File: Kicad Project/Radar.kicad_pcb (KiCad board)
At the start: 2 copper layers, 104.1 x 101.6 mm, 46 parts, among them U1 GALI-1+, U10 GALI-2+, U2 MCA1-85L+, U4 LMV751, U5 LMV751, U6 GALI-2+, U7 RMK-3-93+, U8 GALI-2+, U9 LEE-39+

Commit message: asdf
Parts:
- moved R19 53.5 mm to (163.8, 143.5)
- moved R18 53.1 mm to (181.6, 143.5)
- moved C12 41.8 mm to (134.6, 154.9)
- moved R15 37.8 mm to (147.3, 166.4)
- moved U10 23.8 mm to (185.4, 133.3), turned to 270 degrees
- moved C14 21.6 mm to (188.0, 151.1), turned to 90 degrees
- moved C13 6.62 mm to (174.0, 135.9), turned to 90 degrees
- moved C11 6.00 mm to (188.0, 125.7)
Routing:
- net Net-(C11-Pad1): track 1.23 -> 0.00 mm
- net (no net): track 0.00 -> 1.23 mm
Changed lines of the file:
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@@
     (links 136)
     (no_connects 52)
-    (area 93.904999 76.124999 198.195001 177.875001)
+    (area 93.904999 64.6811 228.422201 177.875001)
     (thickness 1.6)
     (drawings 48)
@@
   )
   (setup
-    (last_trace_width 2.54)
+    (last_trace_width 0.25)
     (user_trace_width 0.254)
     (user_trace_width 0.508)
@@
   )
   (module RadarComponents:Amplifier (layer F.Cu)
-    (at 163.17799 141.9332)
-    (fp_text reference U10 (at -5.9436 -5.9182) (layer F.SilkS)
-      (effects (font (size 1 1) (thickness 0.15)))
-    )
-    (fp_text value GALI-2+ (at 4.1656 -6.1468) (layer F.Fab)
-      (effects (font (size 1 1) (thickness 0.15)))
-    )
-    (pad 2 thru_hole rect (at 0.7874 2.413) (size 1.27 1.27) (drill 0.381) (layers *.Cu *.Mask)
-      (net 9 GND))
-    (pad 2 thru_hole rect (at 2.0574 2.413) (size 1.27 1.27) (drill 0.381) (layers *.Cu *.Mask)
-      (net 9 GND))
-    (pad 2 thru_hole rect (at -0.4826 2.413) (size 1.27 1.27) (drill 0.381) (layers *.Cu *.Mask)
-      (net 9 GND))
-    (pad 2 thru_hole rect (at -0.4826 1.143) (size 1.27 1.27) (drill 0.381) (layers *.Cu *.Mask)
-      (net 9 GND))
-    (pad 2 thru_hole rect (at 0.7874 1.143) (size 1.27 1.27) (drill 0.381) (layers *.Cu *.Mask)
-      (net 9 GND))
-    (pad 2 thru_hole rect (at 2.0574 1.143) (size 1.27 1.27) (drill 0.381) (layers *.Cu *.Mask)
-      (net 9 GND))
-    (pad 2 thru_hole rect (at 2.0828 -4.953) (size 1.27 1.27) (drill 0.381) (layers *.Cu *.Mask)
-      (net 9 GND))
-    (pad 2 thru_hole rect (at 0.8128 -4.953) (size 1.27 1.27) (drill 0.381) (layers *.Cu *.Mask)
-      (net 9 GND))
-    (pad 2 thru_hole rect (at -0.4572 -4.953) (size 1.27 1.27) (drill 0.381) (layers *.Cu *.Mask)
-      (net 9 GND))
-    (pad 2 thru_hole rect (at -0.4572 -3.683) (size 1.27 1.27) (drill 0.381) (layers *.Cu *.Mask)
-      (net 9 GND))
-    (pad 2 thru_hole rect (at 2.0828 -3.683) (size 1.27 1.27) (drill 0.381) (layers *.Cu *.Mask)
-      (net 9 GND))
-    (pad 3 smd rect (at 2.8956 -1.27) (size 2.54 2.54) (layers F.Cu F.Paste F.Mask)
+    (at 185.42 133.35 270)
+    (fp_text reference U10 (at -5.9436 -5.9182 270) (layer F.SilkS)
+      (effects (font (size 1 1) (thickness 0.15)))
+    )
+    (fp_text value GALI-2+ (at 4.1656 -6.1468 270) (layer F.Fab)
+      (effects (font (size 1 1) (thickness 0.15)))
+    )
+    (pad 2 thru_hole rect (at 0.7874 2.413 270) (size 1.27 1.27) (drill 0.381) (layers *.Cu *.Mask)
+      (net 9 GND))
+    (pad 2 thru_hole rect (at 2.0574 2.413 270) (size 1.27 1.27) (drill 0.381) (layers *.Cu *.Mask)
+      (net 9 GND))
+    (pad 2 thru_hole rect (at -0.4826 2.413 270) (size 1.27 1.27) (drill 0.381) (layers *.Cu *.Mask)
+      (net 9 GND))
+    (pad 2 thru_hole rect (at -0.4826 1.143 270) (size 1.27 1.27) (drill 0.381) (layers *.Cu *.Mask)
+      (net 9 GND))
+    (pad 2 thru_hole rect (at 0.7874 1.143 270) (size 1.27 1.27) (drill 0.381) (layers *.Cu *.Mask)
+      (net 9 GND))
+    (pad 2 thru_hole rect (at 2.0574 1.143 270) (size 1.27 1.27) (drill 0.381) (layers *.Cu *.Mask)
+      (net 9 GND))
+    (pad 2 thru_hole rect (at 2.0828 -4.953 270) (size 1.27 1.27) (drill 0.381) (layers *.Cu *.Mask)
+      (net 9 GND))
+    (pad 2 thru_hole rect (at 0.8128 -4.953 270) (size 1.27 1.27) (drill 0.381) (layers *.Cu *.Mask)
+      (net 9 GND))
+    (pad 2 thru_hole rect (at -0.4572 -4.953 270) (size 1.27 1.27) (drill 0.381) (layers *.Cu *.Mask)
+      (net 9 GND))
+    (pad 2 thru_hole rect (at -0.4572 -3.683 270) (size 1.27 1.27) (drill 0.381) (layers *.Cu *.Mask)
+      (net 9 GND))
+    (pad 2 thru_hole rect (at 2.0828 -3.683 270) (size 1.27 1.27) (drill 0.381) (layers *.Cu *.Mask)
+      (net 9 GND))
+    (pad 3 smd rect (at 2.8956 -1.27 270) (size 2.54 2.54) (layers F.Cu F.Paste F.Mask)
       (net 28 "Net-(C14-Pad2)"))
-    (pad 1 smd rect (at -1.27 -1.27) (size 2.54 2.54) (layers F.Cu F.Paste F.Mask)
+    (pad 1 smd rect (at -1.27 -1.27 270) (size 2.54 2.54) (layers F.Cu F.Paste F.Mask)
       (net 17 "Net-(C11-Pad1)"))
-    (pad 2 smd rect (at 0.8128 -1.27) (size 0.635 3.556) (layers F.Cu F.Paste F.Mask)
-      (net 9 GND))
-    (pad 2 thru_hole rect (at 0.8128 -3.683) (size 1.27 1.27) (drill 0.381) (layers *.Cu *.Mask)
+    (pad 2 smd rect (at 0.8128 -1.27 270) (size 0.635 3.556) (layers F.Cu F.Paste F.Mask)
+      (net 9 GND))
+    (pad 2 thru_hole rect (at 0.8128 -3.683 270) (size 1.27 1.27) (drill 0.381) (layers *.Cu *.Mask)
       (net 9 GND))
   )
@@
   )
   (module RadarComponents:100PAD (layer F.Cu)
-    (at 188.5315 131.699 90)
+    (at 187.96 125.73 90)
     (fp_text reference C11 (at -2.9972 -3.683 90) (layer F.SilkS)
       (effects (font (size 1 1) (thickness 0.15)))
@@
   )
   (module RadarComponents:100PAD (layer F.Cu)
-    (at 172.480581 137.2864)
+    (at 134.62 154.94)
     (fp_text reference C12 (at -2.9972 -3.683) (layer F.SilkS)
       (effects (font (size 1 1) (thickness 0.15)))
@@
   )
   (module RadarComponents:100PAD (layer F.Cu)
-    (at 172.480581 142.3364)
-    (fp_text reference C13 (at -2.9972 -3.683) (layer F.SilkS)
-      (effects (font (size 1 1) (thickness 0.15)))
-    )
-    (fp_text value 150p (at 5.842 -3.683) (layer F.Fab)
-      (effects (font (size 1 1) (thickness 0.15)))
-    )
-    (pad 2 smd rect (at 1.9304 -1.27) (size 2.54 2.54) (layers F.Cu F.Paste F.Mask)
-      (net 9 GND))
-    (pad 1 smd rect (at -1.27 -1.27) (size 2.54 2.54) (layers F.Cu F.Paste F.Mask)
+    (at 173.99 135.89 90)
+    (fp_text reference C13 (at -2.9972 -3.683 90) (layer F.SilkS)
+      (effects (font (size 1 1) (thickness 0.15)))
+    )
+    (fp_text value 150p (at 5.842 -3.683 90) (layer F.Fab)
+      (effects (font (size 1 1) (thickness 0.15)))
+    )
+    (pad 2 smd rect (at 1.9304 -1.27 90) (size 2.54 2.54) (layers F.Cu F.Paste F.Mask)
+      (net 9 GND))
+    (pad 1 smd rect (at -1.27 -1.27 90) (size 2.54 2.54) (layers F.Cu F.Paste F.Mask)
       (net 27 "Net-(C13-Pad1)"))
   )
   (module RadarComponents:100PAD (layer F.Cu)
-    (at 175.9712 133.1468)
-    (fp_text reference C14 (at -2.9972 -3.683) (layer F.SilkS)
-      (effects (font (size 1 1) (thickness 0.15)))
-    )
-    (fp_text value 150p (at 5.842 -3.683) (layer F.Fab)
-      (effects (font (size 1 1) (thickness 0.15)))
-    )
-    (pad 2 smd rect (at 1.9304 -1.27) (size 2.54 2.54) (layers F.Cu F.Paste F.Mask)
+    (at 187.96 151.13 90)
+    (fp_text reference C14 (at -2.9972 -3.683 90) (layer F.SilkS)
+      (effects (font (size 1 1) (thickness 0.15)))
+    )
+    (fp_text value 150p (at 5.842 -3.683 90) (layer F.Fab)
+      (effects (font (size 1 1) (thickness 0.15)))
+    )
+    (pad 2 smd rect (at 1.9304 -1.27 90) (size 2.54 2.54) (layers F.Cu F.Paste F.Mask)
       (net 28 "Net-(C14-Pad2)"))
-    (pad 1 smd rect (at -1.27 -1.27) (size 2.54 2.54) (layers F.Cu F.Paste F.Mask)
+    (pad 1 smd rect (at -1.27 -1.27 90) (size 2.54 2.54) (layers F.Cu F.Paste F.Mask)
       (net 29 "Net-(C14-Pad1)"))
   )
@@
   )
   (module RadarComponents:100PAD (layer F.Cu)
-    (at 179.1462 145.8976)
+    (at 147.32 166.37)
     (fp_text reference R15 (at -2.9972 -3.683) (layer F.SilkS)
       (effects (font (size 1 1) (thickness 0.15)))
@@
   )
   (module RadarComponents:100PAD (layer F.Cu)
-    (at 129.021981 150.985)
+    (at 181.61 143.51)
     (fp_text reference R18 (at -2.9972 -3.683) (layer F.SilkS)
       (effects (font (size 1 1) (thickness 0.15)))
@@
   )
   (module RadarComponents:100PAD (layer F.Cu)
-    (at 112.3188 157.988)
+    (at 163.83 143.51)
     (fp_text reference R19 (at -2.9972 -3.683) (layer F.SilkS)
       (effects (font (size 1 1) (thickness 0.15)))
@@
   (gr_line (start 93.98 76.2) (end 198.12 76.2) (angle 90) (layer Edge.Cuts) (width 0.15))
   (gr_line (start 93.98 177.8) (end 93.98 76.2) (angle 90) (layer Edge.Cuts) (width 0.15))
+  (segment (start 161.90799 140.6632) (end 160.6824 140.6632) (width 0.25) (layer F.Cu) (net 0))
   (segment (start 108.458 94.869) (end 104.4702 94.869) (width 2.54) (layer F.Cu) (net 1))
   (segment (start 104.2416 94.6404) (end 104.2416 94.2848) (width 2.54) (layer F.Cu) (net 1))
@@
   (segment (start 121.031 105.0036) (end 121.0437 105.0163) (width 2.54) (layer F.Cu) (net 14))
   (segment (start 170.2181 104.0384) (end 170.2181 110.0201) (width 2.54) (layer F.Cu) (net 15))
-  (segment (start 161.90799 140.6632) (end 160.6824 140.6632) (width 0.25) (layer F.Cu) (net 17))
   (segment (start 133.985 94.869) (end 133.985 91.8972) (width 2.54) (layer F.Cu) (net 24))
   (segment (start 133.985 94.869) (end 131.0386 94.869) (width 2.54) (layer F.Cu) (net 24))
   (segment (start 140.335 94.869) (end 137.1854 94.869) (width 2.54) (layer F.Cu) (net 25))
-  (segment (start 182.9435 118.1862) (end 182.9435 121.3358) (width 2.54) (layer F.Cu) (net 35) (status 400000))
-  (segment (start 181.4703 122.809) (end 178.6509 122.809) (width 2.54) (layer F.Cu) (net 35) (status 800000))
+  (segment (start 182.9435 118.1862) (end 182.9435 121.3358) (width 2.54) (layer F.Cu) (net 35))
+  (segment (start 181.4703 122.809) (end 178.6509 122.809) (width 2.54) (layer F.Cu) (net 35))
   (segment (start 182.9435 121.3358) (end 181.4703 122.809) (width 2.54) (layer F.Cu) (net 35))
   (segment (start 134.0358 85.5472) (end 134.0358 88.646) (width 2.54) (layer F.Cu) (net 37) (status 20))
-  (segment (start 176.3776 100.838) (end 183.7055 100.838) (width 2.54) (layer F.Cu) (net 39) (status 400000))
-  (segment (start 184.8231 101.9556) (end 184.8231 104.5718) (width 2.54) (layer F.Cu) (net 39) (status 800000))
+  (segment (start 176.3776 100.838) (end 183.7055 100.838) (width 2.54) (layer F.Cu) (net 39))
+  (segment (start 184.8231 101.9556) (end 184.8231 104.5718) (width 2.54) (layer F.Cu) (net 39))
   (segment (start 183.7055 100.838) (end 184.8231 101.9556) (width 2.54) (layer F.Cu) (net 39))
   (zone (net 9) (net_name GND) (layer B.Cu) (hatch edge 0.508)

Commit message: pcb stuff
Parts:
- moved C14 8.89 mm to (188.0, 142.2)
- moved C13 6.98 mm to (181.0, 135.9)
- moved R18 5.99 mm to (184.8, 138.4)
- moved R19 5.08 mm to (163.8, 138.4)
- moved U10 2.54 mm to (185.4, 130.8)
- moved C11 1.27 mm to (188.0, 124.5)
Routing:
- net Net-(C13-Pad1): track 0.00 -> 17.8 mm
- net Net-(C14-Pad2): track 0.00 -> 6.60 mm
- net PowerSplitter: track 8.05 -> 12.3 mm
- net Net-(C11-Pad1): track 0.00 -> 3.81 mm
- net (no net): track 1.23 -> 0.00 mm
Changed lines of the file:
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@@
   (general
     (links 136)
-    (no_connects 52)
+    (no_connects 47)
     (area 93.904999 64.6811 228.422201 177.875001)
     (thickness 1.6)
     (drawings 48)
-    (tracks 56)
+    (tracks 61)
     (zones 0)
     (modules 46)
@@
   )
   (setup
-    (last_trace_width 0.25)
+    (last_trace_width 1.27)
     (user_trace_width 0.254)
     (user_trace_width 0.508)
@@
     (user_trace_width 2.54)
     (trace_clearance 0.2)
-    (zone_clearance 0)
+    (zone_clearance 0.508)
     (zone_45_only yes)
     (trace_min 0.2)
@@
     (mod_text_size 1 1)
     (mod_text_width 0.15)
-    (pad_size 1.524 1.524)
-    (pad_drill 0.762)
+    (pad_size 1.27 1.27)
+    (pad_drill 0.381)
     (pad_to_mask_clearance 0.2)
     (aux_axis_origin 0 0)
@@
     (add_net RFIN)
   )
+  (module RadarComponents:100PAD (layer F.Cu)
+    (at 180.975 135.89 90)
+    (fp_text reference C13 (at -2.9972 -3.683 90) (layer F.SilkS)
+      (effects (font (size 1 1) (thickness 0.15)))
+    )
+    (fp_text value 150p (at 5.842 -3.683 90) (layer F.Fab)
+      (effects (font (size 1 1) (thickness 0.15)))
+    )
+    (pad 2 smd rect (at 1.9304 -1.27 90) (size 2.54 2.54) (layers F.Cu F.Paste F.Mask)
+      (net 9 GND))
+    (pad 1 smd rect (at -1.27 -1.27 90) (size 2.54 2.54) (layers F.Cu F.Paste F.Mask)
+      (net 27 "Net-(C13-Pad1)"))
+  )
   (module RadarComponents:Amplifier (layer F.Cu)
     (at 168.6687 121.5263 180)
@@
   )
   (module RadarComponents:Amplifier (layer F.Cu)
-    (at 185.42 133.35 270)
+    (at 185.42 130.81 270)
     (fp_text reference U10 (at -5.9436 -5.9182 270) (layer F.SilkS)
       (effects (font (size 1 1) (thickness 0.15)))
@@
   )
   (module RadarComponents:100PAD (layer F.Cu)
-    (at 187.96 125.73 90)
+    (at 187.96 124.46 90)
     (fp_text reference C11 (at -2.9972 -3.683 90) (layer F.SilkS)
       (effects (font (size 1 1) (thickness 0.15)))
@@
   )
   (module RadarComponents:100PAD (layer F.Cu)
-    (at 173.99 135.89 90)
-    (fp_text reference C13 (at -2.9972 -3.683 90) (layer F.SilkS)
-      (effects (font (size 1 1) (thickness 0.15)))
-    )
-    (fp_text value 150p (at 5.842 -3.683 90) (layer F.Fab)
-      (effects (font (size 1 1) (thickness 0.15)))
-    )
-    (pad 2 smd rect (at 1.9304 -1.27 90) (size 2.54 2.54) (layers F.Cu F.Paste F.Mask)
-      (net 9 GND))
-    (pad 1 smd rect (at -1.27 -1.27 90) (size 2.54 2.54) (layers F.Cu F.Paste F.Mask)
-      (net 27 "Net-(C13-Pad1)"))
-  )
-  (module RadarComponents:100PAD (layer F.Cu)
-    (at 187.96 151.13 90)
+    (at 187.96 142.24 90)
     (fp_text reference C14 (at -2.9972 -3.683 90) (layer F.SilkS)
       (effects (font (size 1 1) (thickness 0.15)))
@@
   )
   (module RadarComponents:100PAD (layer F.Cu)
-    (at 181.61 143.51)
+    (at 184.785 138.43)
     (fp_text reference R18 (at -2.9972 -3.683) (layer F.SilkS)
       (effects (font (size 1 1) (thickness 0.15)))
@@
   )
   (module RadarComponents:100PAD (layer F.Cu)
-    (at 163.83 143.51)
+    (at 163.83 138.43)
     (fp_text reference R19 (at -2.9972 -3.683) (layer F.SilkS)
       (effects (font (size 1 1) (thickness 0.15)))
@@
   (gr_line (start 93.98 76.2) (end 198.12 76.2) (angle 90) (layer Edge.Cuts) (width 0.15))
   (gr_line (start 93.98 177.8) (end 93.98 76.2) (angle 90) (layer Edge.Cuts) (width 0.15))
-  (segment (start 161.90799 140.6632) (end 160.6824 140.6632) (width 0.25) (layer F.Cu) (net 0))
   (segment (start 108.458 94.869) (end 104.4702 94.869) (width 2.54) (layer F.Cu) (net 1))
   (segment (start 104.2416 94.6404) (end 104.2416 94.2848) (width 2.54) (layer F.Cu) (net 1))
@@
   (segment (start 121.031 105.0036) (end 121.0437 105.0163) (width 2.54) (layer F.Cu) (net 14))
   (segment (start 170.2181 104.0384) (end 170.2181 110.0201) (width 2.54) (layer F.Cu) (net 15))
+  (segment (start 186.69 125.73) (end 186.69 129.54) (width 2.54) (layer F.Cu) (net 17))
   (segment (start 133.985 94.869) (end 133.985 91.8972) (width 2.54) (layer F.Cu) (net 24))
   (segment (start 133.985 94.869) (end 131.0386 94.869) (width 2.54) (layer F.Cu) (net 24))
   (segment (start 140.335 94.869) (end 137.1854 94.869) (width 2.54) (layer F.Cu) (net 25))
+  (segment (start 183.515 137.16) (end 179.705 137.16) (width 1.27) (layer F.Cu) (net 27) (status C00000))
+  (segment (start 179.705 137.16) (end 165.7604 137.16) (width 1.27) (layer F.Cu) (net 27) (status C00000))
+  (segment (start 186.69 133.7056) (end 186.69 140.3096) (width 2.54) (layer F.Cu) (net 28))
+  (segment (start 186.69 122.5296) (end 186.69 118.3767) (width 2.54) (layer F.Cu) (net 35))
+  (segment (start 186.69 118.3767) (end 186.7789 118.2878) (width 2.54) (layer F.Cu) (net 35))
   (segment (start 182.9435 118.1862) (end 182.9435 121.3358) (width 2.54) (layer F.Cu) (net 35))
   (segment (start 181.4703 122.809) (end 178.6509 122.809) (width 2.54) (layer F.Cu) (net 35))

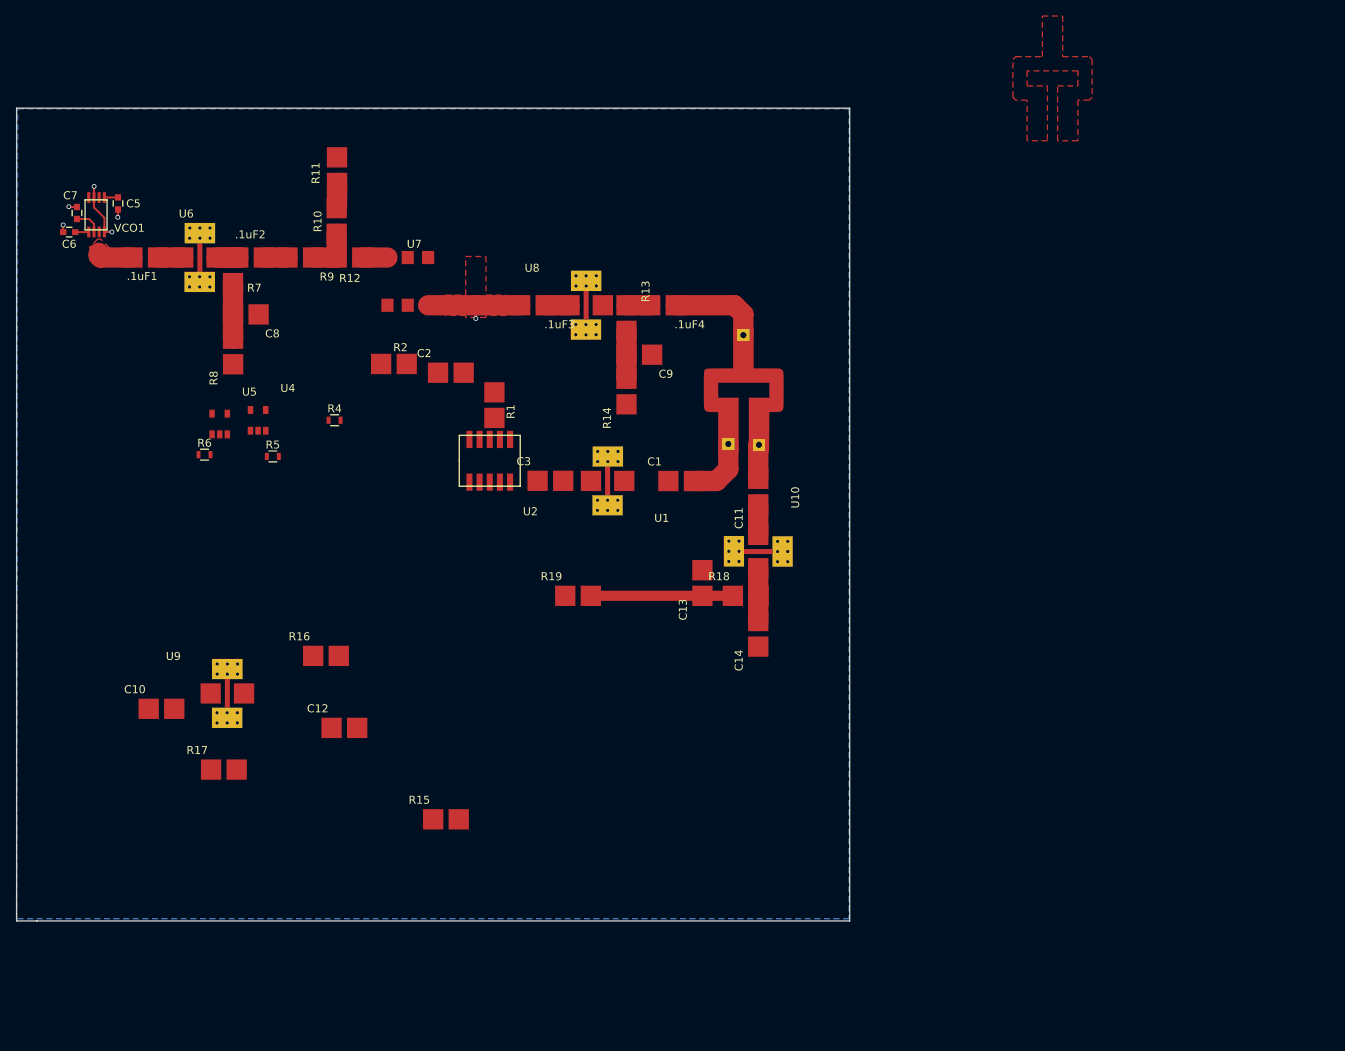
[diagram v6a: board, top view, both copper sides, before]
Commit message: Added Filters to PCB
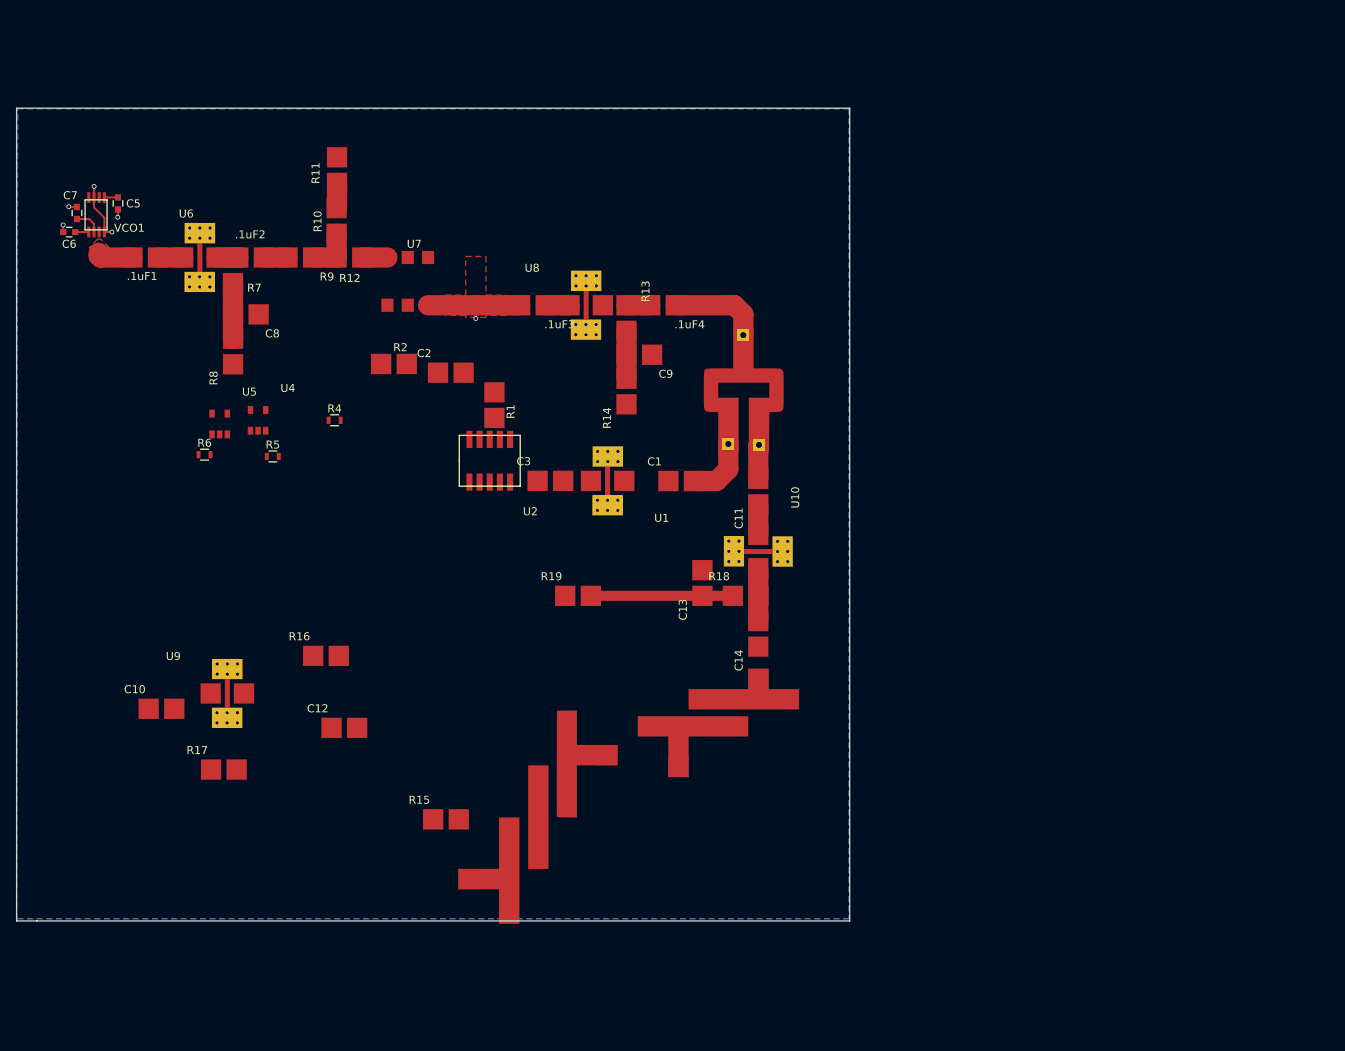
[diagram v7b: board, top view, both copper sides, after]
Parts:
- added U11: BandpassFilter, RadarComponents:DoubleFilter, F.Cu at (180.9, 155.7)
- added U3: BandpassFilter, RadarComponents:QuadPoleFilter, F.Cu at (158.8, 164.9)
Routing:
- removed copper zone on F.Cu, net /SourceModule.sch/PowerSplitter
